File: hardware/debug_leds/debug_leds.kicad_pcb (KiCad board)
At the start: 4 copper layers, 58.4 x 25.4 mm, 29 parts, among them J1 Conn_01x20, J2 Conn_01x20, U1 74HC04, U2 74HC04, U3 74HC04

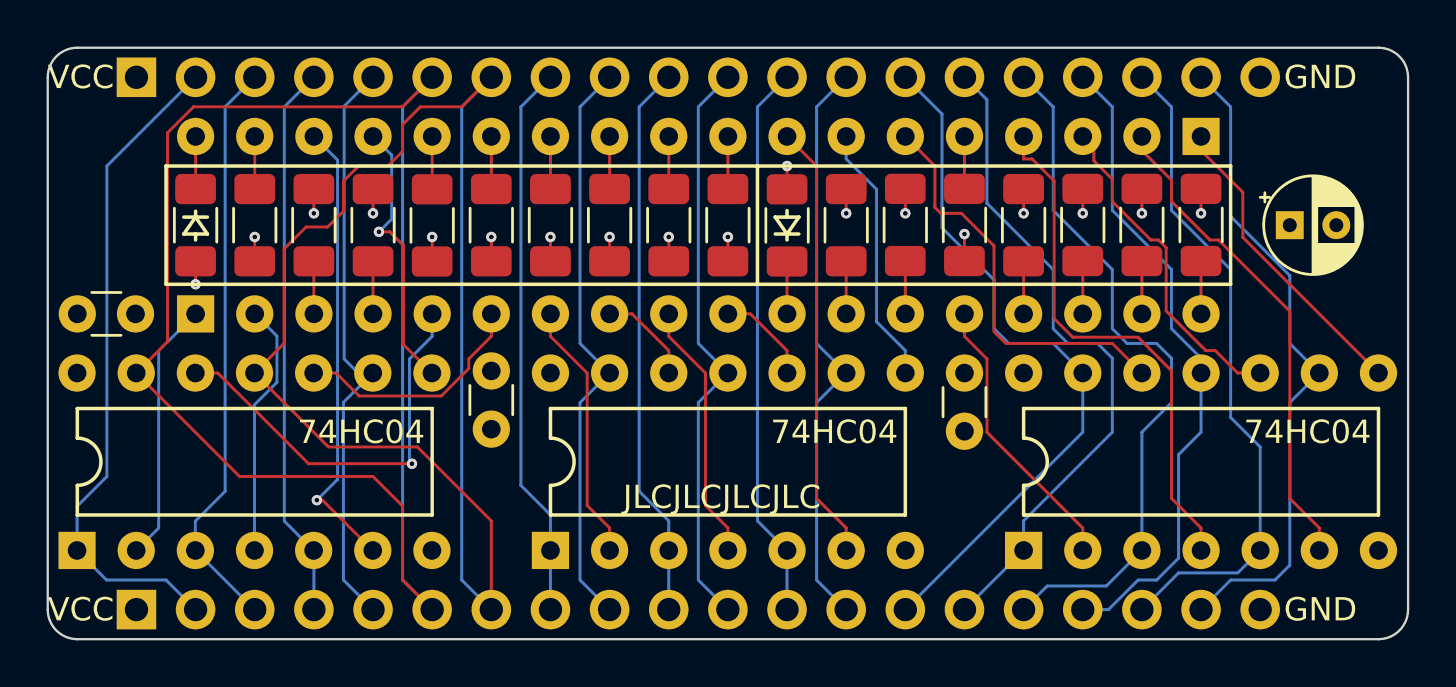
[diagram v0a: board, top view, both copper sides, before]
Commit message: Update debug leds
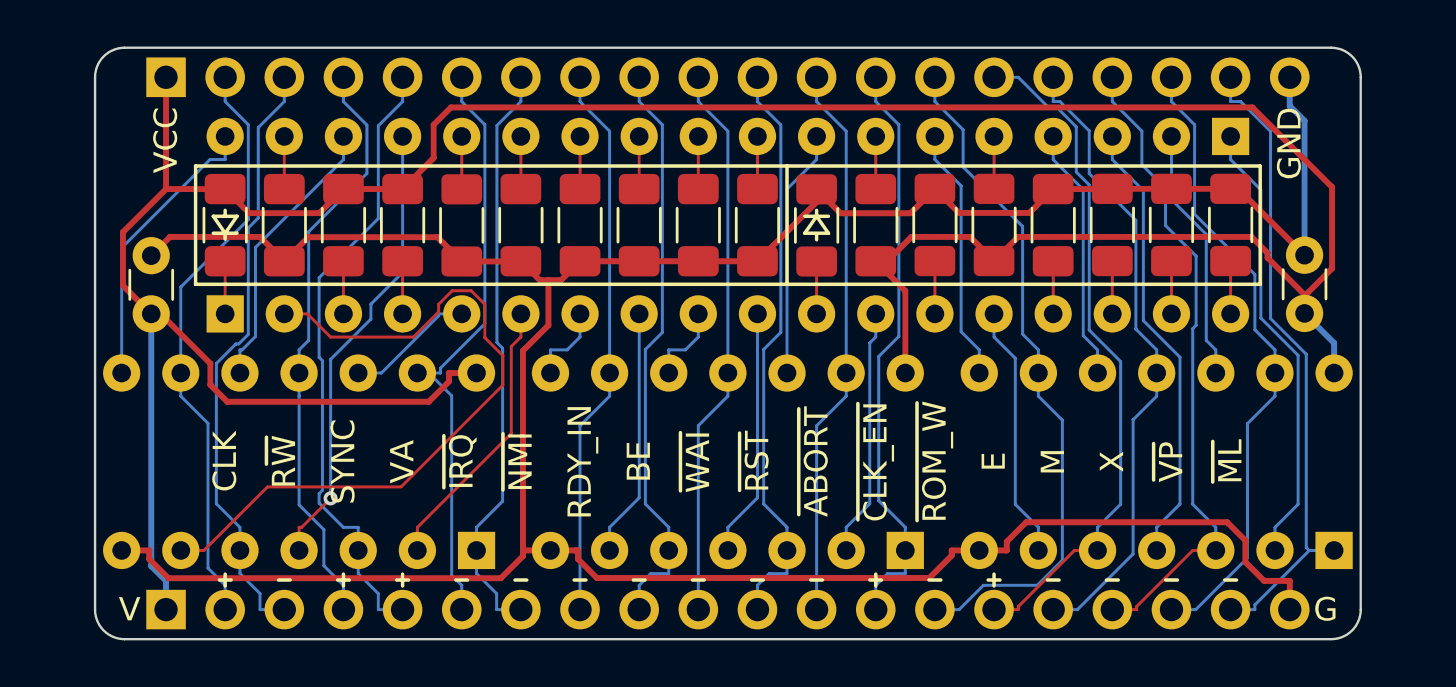
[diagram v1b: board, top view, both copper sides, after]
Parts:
- removed the C1 at (154.9, 58.4)
- removed C4: 100n, Capacitor_THT:C_Disc_D3.0mm_W1.6mm_P2.50mm
- J1, J2, U1, U2, U3: moved to B.Cu
- moved C1 35.0 mm to (155.6, 62.2), turned to 90 degrees
- moved U1 17.2 mm to (120.0, 72.4)
- moved U2 15.2 mm to (138.4, 72.4)
- moved U3 13.3 mm to (156.8, 72.4)
- moved C2 3.17 mm to (106.0, 62.2), turned to 90 degrees
- moved BAR2 1.27 mm to (152.4, 54.6)
- moved J1 1.27 mm to (106.7, 74.9), turned to -90 degrees
- moved J2 1.27 mm to (106.7, 52.1), turned to -90 degrees
- moved R10 1.27 mm to (132.1, 58.4)
- moved R11 1.27 mm to (134.6, 58.4)
- moved R12 1.27 mm to (137.2, 58.4)
- moved R14 1.27 mm to (142.2, 58.4)
- moved R15 1.27 mm to (144.8, 58.4)
- moved R17 1.27 mm to (149.9, 58.4)
- moved R18 1.27 mm to (152.4, 58.4)
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- renumbered C2 to C1, C3 to C2
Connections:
- BAR1 pad 1: Net-(U1-Pad2) -> Net-(BAR1-A-Pad1)
- BAR1 pad 10: Net-(U2-Pad10) -> Net-(U2-Y2)
- BAR1 pad 17: Net-(U1-Pad8) -> Net-(U1-Y2)
- BAR1 pad 18: Net-(U1-Pad6) -> Net-(U1-Y5)
- BAR1 pad 2: Net-(U1-Pad4) -> Net-(U1-Y3)
- BAR1 pad 20: Net-(BAR1-Pad20) -> Net-(U1-Y4)
- BAR1 pad 6: Net-(U1-Pad10) -> Net-(U1-Y1)
- BAR1 pad 7: Net-(U2-Pad2) -> Net-(U2-Y4)
- BAR1 pad 8: Net-(U2-Pad12) -> Net-(U2-Y3)
- BAR1 pad 9: Net-(U2-Pad4) -> Net-(U2-Y5)
- BAR2 pad 1: Net-(BAR2-Pad1) -> Net-(U3-Y1)
- BAR2 pad 10: Net-(BAR2-Pad10) -> Net-(U2-Y1)
- BAR2 pad 12: Net-(U3-Pad2) -> Net-(U3-Y3)
- BAR2 pad 2: Net-(U3-Pad6) -> Net-(U3-Y6)
- BAR2 pad 3: Net-(U3-Pad10) -> Net-(U3-Y2)
- BAR2 pad 4: Net-(U3-Pad4) -> Net-(U3-Y5)
- BAR2 pad 6: Net-(U3-Pad12) -> Net-(U3-Y4)
- BAR2 pad 7: Net-(U2-Pad8) -> Net-(BAR2-A-Pad7)
- BAR2 pad 8: Net-(U2-Pad6) -> Net-(U2-Y6)
- R1 pad 1: Net-(BAR1-Pad20) -> VCC
- R1 pad 2: GND -> Net-(BAR1-A-Pad1)
- R12 pad 1: Net-(BAR2-Pad10) -> VCC
- R12 pad 2: GND -> Net-(BAR2-A-Pad7)
- U1 pad 1: /CLK -> /~{NMI}
- U1 pad 10: Net-(U1-Pad10) -> Net-(U1-Y5)
- U1 pad 11: /~{NMI} -> /SYNC
- U1 pad 2: Net-(U1-Pad2) -> Net-(U1-Y1)
- U1 pad 3: /R~{W} -> /VA
- U1 pad 4: Net-(U1-Pad4) -> Net-(U1-Y2)
- U1 pad 5: /SYNC -> /R~{W}
- U1 pad 6: Net-(U1-Pad6) -> Net-(U1-Y3)
- U1 pad 8: Net-(U1-Pad8) -> Net-(U1-Y4)
- U1 pad 9: /VA -> /CLK
- U2 pad 1: /RDY_IN -> /~{CLK_EN}
- U2 pad 10: Net-(U2-Pad10) -> Net-(U2-Y5)
- U2 pad 11: /~{RST} -> /~{WAI}
- U2 pad 12: Net-(U2-Pad12) -> Net-(U2-Y6)
- U2 pad 13: /BE -> /~{ABORT}
- U2 pad 2: Net-(U2-Pad2) -> Net-(U2-Y1)
- U2 pad 3: /~{WAI} -> /~{RST}
- U2 pad 4: Net-(U2-Pad4) -> Net-(U2-Y2)
- U2 pad 5: /~{ABORT} -> /BE
- U2 pad 6: Net-(U2-Pad6) -> Net-(U2-Y3)
- U2 pad 8: Net-(U2-Pad8) -> Net-(U2-Y4)
- U2 pad 9: /~{CLK_EN} -> /RDY_IN
- U3 pad 1: /E -> /~{ML}
- U3 pad 10: Net-(U3-Pad10) -> Net-(U3-Y5)
- U3 pad 11: /X -> /M
- U3 pad 12: Net-(U3-Pad12) -> Net-(U3-Y6)
- U3 pad 13: /~{ROM_WE} -> /~{VP}
- U3 pad 2: Net-(U3-Pad2) -> Net-(U3-Y1)
- U3 pad 3: /M -> /X
- U3 pad 4: Net-(U3-Pad4) -> Net-(U3-Y2)
- U3 pad 5: /~{VP} -> /E
- U3 pad 6: Net-(U3-Pad6) -> Net-(U3-Y3)
- U3 pad 8: Net-(BAR2-Pad1) -> Net-(U3-Y4)
- U3 pad 9: /~{ML} -> /~{ROM_WE}
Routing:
- net VCC: track 3.24 -> 130.9 mm, vias 3 -> 0
- net GND: track 15.6 -> 132.5 mm, vias 15 -> 0
- net /~{IRQ}: track 65.9 -> 25.6 mm
- net /~{NMI}: track 59.8 -> 25.3 mm
- net Net-(U1-Y3): track 0.00 -> 30.8 mm
- net Net-(U3-Pad4): track 22.8 -> 0.00 mm
- net Net-(U3-Pad6): track 21.2 -> 0.00 mm
- net Net-(U1-Pad6): track 19.7 -> 0.00 mm, vias 1 -> 0
- net Net-(U1-Y2): track 0.00 -> 19.7 mm, vias 0 -> 1
- net Net-(U3-Y2): track 0.00 -> 19.4 mm
- net Net-(U3-Y1): track 0.00 -> 19.4 mm
- net Net-(U2-Pad6): track 18.8 -> 0.00 mm
- net Net-(U3-Pad12): track 17.6 -> 0.00 mm
- net Net-(U3-Pad10): track 14.3 -> 0.00 mm
- net Net-(BAR2-Pad1): track 13.3 -> 0.00 mm
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- removed copper zone on In2.Cu, net GND
- removed copper zone on In1.Cu, net VCC
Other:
- board size 58.4 x 25.4 mm -> 54.4 x 25.4 mm
- copper layers 4 -> 2
- board text added: "65816 Debug LEDs 2023-08-05 - Rev B A. Kohlbecker"
- board text added: "BE"
- board text added: "CLK"
- board text added: "E"
- board text added: "G"
- board text added: "M"
- board text added: "RDY_IN"
- board text added: "R~{W}"
- board text added: "SYNC"
- board text added: "V"
- board text added: "VA"
- board text added: "X"
- board text added: "~{ABORT}"
- board text added: "~{CLK_EN}"
- board text added: "~{IRQ}"
- board text added: "~{ML}"
- board text added: "~{NMI}"
- board text added: "~{ROM_W}"
- board text added: "~{RST}"
- board text added: "~{VP}"
- board text added: "~{WAI}"
- board text removed: "65816 Debug LEDs 2023-06-10 - Rev A A. Kohlbecker"
